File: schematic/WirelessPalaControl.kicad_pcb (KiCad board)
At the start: 2 copper layers, 26.7 x 35.1 mm, 20 parts, among them J1 6P6C, J2 MCU UART, Q1 BC847B, Q2 BC847B, U1 SI8621, U2 WeMos_mini

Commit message: Update schematic
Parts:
- C1, C2: footprint Capacitors_SMD:C_0805_HandSoldering -> Capacitor_SMD:C_0805_2012Metric_Pad1.15x1.40mm_HandSolder
- D1, D3: footprint LEDs:LED_0805_HandSoldering -> LED_SMD:LED_0805_2012Metric_Pad1.15x1.40mm_HandSolder
- D2: footprint Diodes_SMD:D_SMA -> Diode_SMD:D_SMA
- J2: footprint Pin_Headers:Pin_Header_Straight_1x04_Pitch2.54mm -> Connector_PinHeader_2.54mm:PinHeader_1x04_P2.54mm_Vertical
- Q1, Q2: footprint TO_SOT_Packages_SMD:SOT-23_Handsoldering -> Package_TO_SOT_SMD:SOT-23_Handsoldering
- R1, R2, R3, R4, R5, R6, R7, R8: footprint Resistors_SMD:R_0805_HandSoldering -> Resistor_SMD:R_0805_2012Metric_Pad1.15x1.40mm_HandSolder
- U1: footprint Housings_SOIC:SOIC-8_3.9x4.9mm_Pitch1.27mm -> Package_SO:SOIC-8_3.9x4.9mm_P1.27mm
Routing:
- net /GND2: track 40.5 -> 39.1 mm
- net Net-(D1-Pad2): track 18.5 -> 17.9 mm
- net /VDD1: track 37.8 -> 37.2 mm
- net Net-(D2-Pad1): track 15.4 -> 16.0 mm

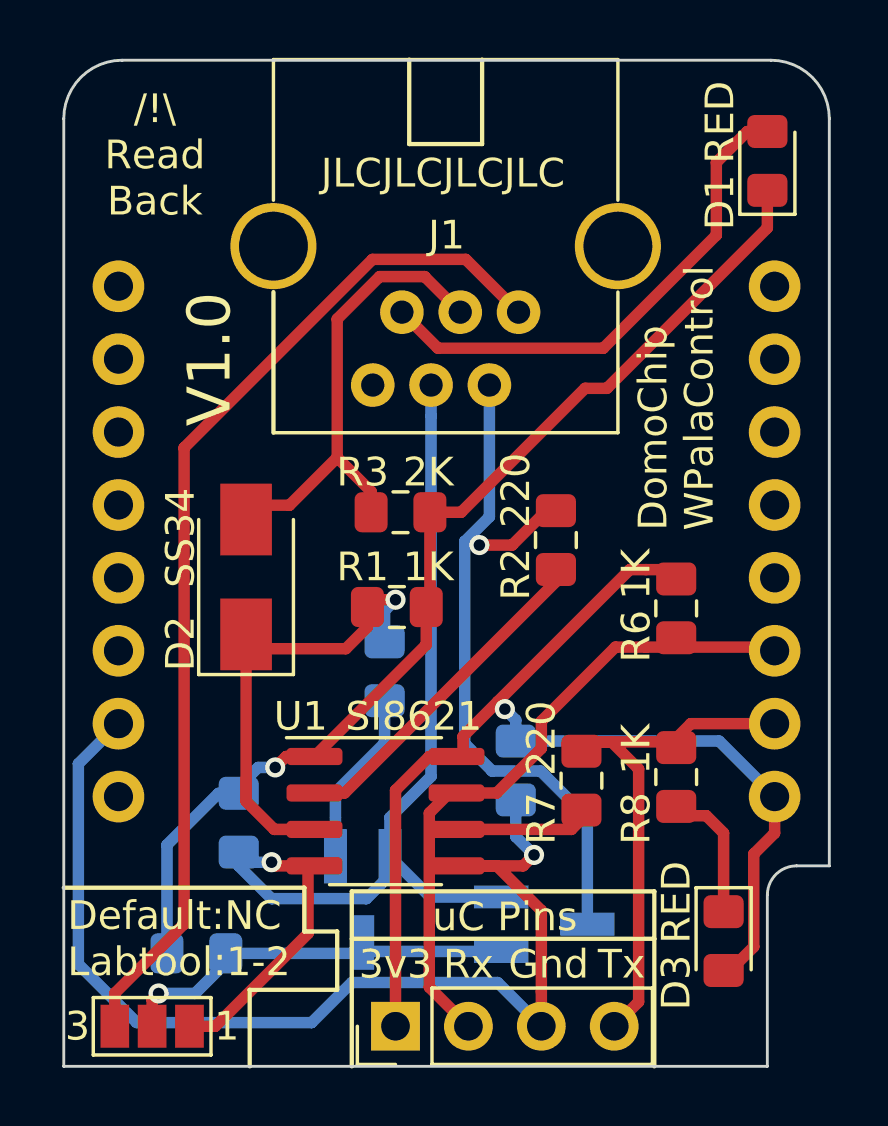
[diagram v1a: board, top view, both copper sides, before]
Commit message: Update schematic fix rj12
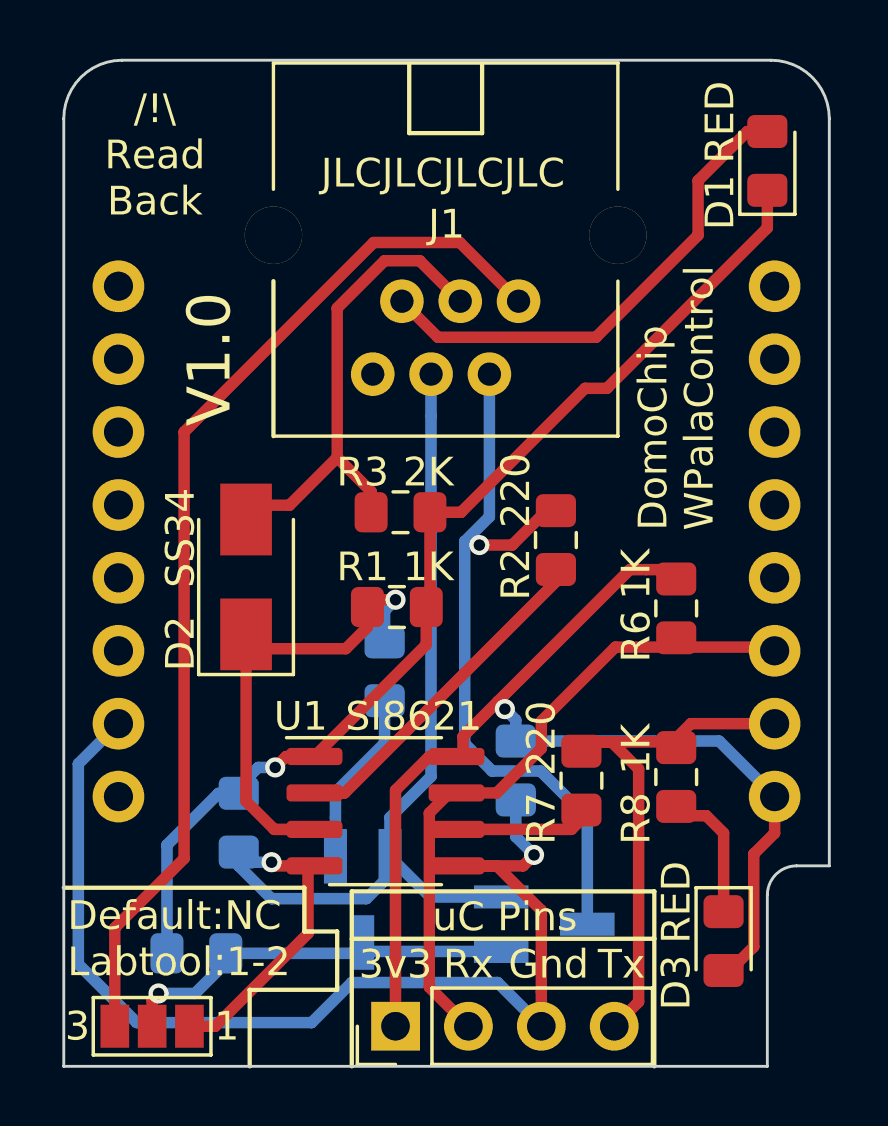
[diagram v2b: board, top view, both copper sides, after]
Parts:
- moved J1 0.38 mm to (36.2, 30.0)
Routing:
- net Net-(J1-Pad6): track 36.3 -> 36.9 mm
- net Net-(D1-Pad2): track 17.9 -> 17.3 mm
- net /Rx: track 16.5 -> 17.0 mm
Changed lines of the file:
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@@
     (add_net "Net-(R7-Pad2)")
+  )
+  (module MyRJ:Ali_RJ12 (layer F.Cu)
+    (at 36.164 29.972 180)
+    (fp_text reference J1 (at -0.031 0.381) (layer F.SilkS)
+      (effects (font (size 1 1) (thickness 0.15)))
+    )
+    (fp_text value 6P6C (at 0 1.778) (layer F.Fab)
+      (effects (font (size 1 1) (thickness 0.15)))
+    )
+    (fp_line (start 1.27 3.556) (end 1.27 6) (layer F.SilkS) (width 0.15))
+    (fp_line (start -1.27 3.556) (end 1.27 3.556) (layer F.SilkS) (width 0.15))
+    (fp_line (start -1.27 6) (end -1.27 3.556) (layer F.SilkS) (width 0.15))
+    (fp_line (start 6 -7) (end 6 -1.6) (layer F.SilkS) (width 0.15))
+    (fp_line (start -6 -7) (end -6 -1.6) (layer F.SilkS) (width 0.12))
+    (fp_line (start -6 6) (end 6 6) (layer F.SilkS) (width 0.12))
+    (fp_line (start -6 -7) (end 6 -7) (layer F.SilkS) (width 0.12))
+    (fp_line (start -6 1.6) (end -6 6) (layer F.SilkS) (width 0.12))
+    (fp_line (start 6 1.6) (end 6 6) (layer F.SilkS) (width 0.12))
+    (pad 5 thru_hole circle (at -1.524 -4.84) (size 1.52 1.52) (drill 0.81) (layers *.Cu *.Mask)
+      (net 9 /Tx-RxH))
+    (pad 1 thru_hole circle (at 2.54 -4.84) (size 1.52 1.52) (drill 0.81) (layers *.Cu *.Mask))
+    (pad 3 thru_hole circle (at 0.508 -4.84) (size 1.52 1.52) (drill 0.81) (layers *.Cu *.Mask)
+      (net 2 /GND1))
+    (pad 4 thru_hole circle (at -0.508 -2.3) (size 1.52 1.52) (drill 0.81) (layers *.Cu *.Mask)
+      (net 6 /Rx))
+    (pad 2 thru_hole circle (at 1.524 -2.3) (size 1.52 1.52) (drill 0.81) (layers *.Cu *.Mask)
+      (net 5 "Net-(D1-Pad2)"))
+    (pad 6 thru_hole circle (at -2.54 -2.3) (size 1.52 1.52) (drill 0.81) (layers *.Cu *.Mask)
+      (net 16 "Net-(J1-Pad6)"))
+    (pad "" thru_hole circle (at 6 0 180) (size 2 2) (drill 2) (layers *.Cu *.Mask))
+    (pad "" thru_hole circle (at -6 0 180) (size 2 2) (drill 2) (layers *.Cu *.Mask))
   )
   (module wemos_d1_mini:wemos-d1-mini-DIL-only (layer B.Cu)
@@
     (pad 1 smd rect (at -1.3 0 180) (size 1 1.5) (layers F.Cu F.Mask)
       (net 2 /GND1))
-  )
-  (module MyRJ:Ali_RJ12 (layer F.Cu)
-    (at 36.164 30.353 180)
-    (fp_text reference J1 (at -0.031 0.381) (layer F.SilkS)
-      (effects (font (size 1 1) (thickness 0.15)))
-    )
-    (fp_text value 6P6C (at 0 1.778) (layer F.Fab)
-      (effects (font (size 1 1) (thickness 0.15)))
-    )
-    (fp_line (start 6 1.6) (end 6 6.5) (layer F.SilkS) (width 0.12))
-    (fp_line (start -6 1.6) (end -6 6.5) (layer F.SilkS) (width 0.12))
-    (fp_line (start -6 -6.5) (end 6 -6.5) (layer F.SilkS) (width 0.12))
-    (fp_line (start -6 6.5) (end 6 6.5) (layer F.SilkS) (width 0.12))
-    (fp_line (start -6 -6.5) (end -6 -1.6) (layer F.SilkS) (width 0.12))
-    (fp_line (start 6 -6.5) (end 6 -1.6) (layer F.SilkS) (width 0.15))
-    (fp_line (start -1.27 6.5) (end -1.27 3.556) (layer F.SilkS) (width 0.15))
-    (fp_line (start -1.27 3.556) (end 1.27 3.556) (layer F.SilkS) (width 0.15))
-    (fp_line (start 1.27 3.556) (end 1.27 6.5) (layer F.SilkS) (width 0.15))
-    (pad "" np_thru_hole circle (at -6 0 180) (size 3 3) (drill 2.4) (layers *.Cu *.Mask))
-    (pad "" np_thru_hole circle (at 6 0 180) (size 3 3) (drill 2.4) (layers *.Cu *.Mask))
-    (pad 6 thru_hole circle (at -2.54 -2.3) (size 1.52 1.52) (drill 0.81) (layers *.Cu *.Mask)
-      (net 16 "Net-(J1-Pad6)"))
-    (pad 2 thru_hole circle (at 1.524 -2.3) (size 1.52 1.52) (drill 0.81) (layers *.Cu *.Mask)
-      (net 5 "Net-(D1-Pad2)"))
-    (pad 4 thru_hole circle (at -0.508 -2.3) (size 1.52 1.52) (drill 0.81) (layers *.Cu *.Mask)
-      (net 6 /Rx))
-    (pad 3 thru_hole circle (at 0.508 -4.84) (size 1.52 1.52) (drill 0.81) (layers *.Cu *.Mask)
-      (net 2 /GND1))
-    (pad 1 thru_hole circle (at 2.54 -4.84) (size 1.52 1.52) (drill 0.81) (layers *.Cu *.Mask))
-    (pad 5 thru_hole circle (at -1.524 -4.84) (size 1.52 1.52) (drill 0.81) (layers *.Cu *.Mask)
-      (net 9 /Tx-RxH))
   )
   (module Capacitor_SMD:C_0805_2012Metric_Pad1.15x1.40mm_HandSolder (layer B.Cu)
@@
   (segment (start 45.691 47.596) (end 38.608 47.596) (width 0.4) (layer B.Cu) (net 4))
   (segment (start 47.625 49.53) (end 45.691 47.596) (width 0.4) (layer B.Cu) (net 4))
-  (segment (start 34.64 32.653) (end 35.896 33.909) (width 0.4) (layer F.Cu) (net 5))
-  (segment (start 35.896 33.909) (end 41.656 33.909) (width 0.4) (layer F.Cu) (net 5))
-  (segment (start 41.656 33.909) (end 45.593 29.972) (width 0.4) (layer F.Cu) (net 5))
+  (segment (start 34.64 32.272) (end 35.896 33.528) (width 0.4) (layer F.Cu) (net 5))
+  (segment (start 35.896 33.528) (end 41.402 33.528) (width 0.4) (layer F.Cu) (net 5))
+  (segment (start 41.402 33.528) (end 44.958 29.972) (width 0.4) (layer F.Cu) (net 5))
   (segment (start 46.671 26.36) (end 47.371 26.36) (width 0.4) (layer F.Cu) (net 5))
-  (segment (start 45.593 27.438) (end 46.671 26.36) (width 0.4) (layer F.Cu) (net 5))
-  (segment (start 45.593 29.972) (end 45.593 27.438) (width 0.4) (layer F.Cu) (net 5))
-  (segment (start 36.672 32.653) (end 35.433 31.414) (width 0.4) (layer F.Cu) (net 6))
-  (segment (start 35.433 31.414) (end 33.864 31.414) (width 0.4) (layer F.Cu) (net 6))
-  (segment (start 33.864 31.414) (end 32.385 32.893) (width 0.4) (layer F.Cu) (net 6))
-  (segment (start 32.385 32.893) (end 32.385 37.718) (width 0.4) (layer F.Cu) (net 6))
+  (segment (start 44.958 28.073) (end 46.671 26.36) (width 0.4) (layer F.Cu) (net 5))
+  (segment (start 44.958 29.972) (end 44.958 28.073) (width 0.4) (layer F.Cu) (net 5))
   (segment (start 33.566 38.899) (end 33.566 39.624) (width 0.4) (layer F.Cu) (net 6))
   (segment (start 32.385 37.718) (end 33.566 38.899) (width 0.4) (layer F.Cu) (net 6))
   (segment (start 30.725 39.378) (end 29.21 39.378) (width 0.4) (layer F.Cu) (net 6))
   (segment (start 32.385 37.718) (end 30.725 39.378) (width 0.4) (layer F.Cu) (net 6))
+  (segment (start 36.672 32.272) (end 35.261 30.861) (width 0.4) (layer F.Cu) (net 6))
+  (segment (start 35.261 30.861) (end 34.036 30.861) (width 0.4) (layer F.Cu) (net 6))
+  (segment (start 32.385 32.512) (end 32.385 37.718) (width 0.4) (layer F.Cu) (net 6))
+  (segment (start 34.036 30.861) (end 32.385 32.512) (width 0.4) (layer F.Cu) (net 6))
   (segment (start 30.194 50.673) (end 31.369 50.673) (width 0.4) (layer F.Cu) (net 7))
   (segment (start 29.21 49.689) (end 30.194 50.673) (width 0.4) (layer F.Cu) (net 7))
@@
   (segment (start 40.546 50.673) (end 40.894 50.325) (width 0.4) (layer F.Cu) (net 15))
   (segment (start 36.769 50.673) (end 40.546 50.673) (width 0.4) (layer F.Cu) (net 15))
-  (segment (start 33.615467 30.813991) (end 27.051 37.378458) (width 0.4) (layer F.Cu) (net 16))
-  (segment (start 38.704 32.653) (end 36.864991 30.813991) (width 0.4) (layer F.Cu) (net 16))
-  (segment (start 36.864991 30.813991) (end 33.615467 30.813991) (width 0.4) (layer F.Cu) (net 16))
-  (segment (start 24.638 56.381) (end 24.638 57.531) (width 0.4) (layer F.Cu) (net 16))
-  (segment (start 27.051 53.968) (end 24.638 56.381) (width 0.4) (layer F.Cu) (net 16))
-  (segment (start 27.051 37.378458) (end 27.051 53.968) (width 0.4) (layer F.Cu) (net 16))
+  (segment (start 38.704 32.272) (end 36.658 30.226) (width 0.4) (layer F.Cu) (net 16))
+  (segment (start 36.658 30.226) (end 33.655 30.226) (width 0.4) (layer F.Cu) (net 16))
+  (segment (start 33.655 30.226) (end 27.051 36.83) (width 0.4) (layer F.Cu) (net 16))
+  (segment (start 27.051 36.83) (end 27.051 51.689) (width 0.4) (layer F.Cu) (net 16))
+  (segment (start 24.638 54.102) (end 24.638 57.531) (width 0.4) (layer F.Cu) (net 16))
+  (segment (start 27.051 51.689) (end 24.638 54.102) (width 0.4) (layer F.Cu) (net 16))
 )

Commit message: Update PCB fix size V1.1
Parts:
- moved D1 2.41 mm to (45.5, 25.9), turned to 180 degrees
- moved JP1 1.88 mm to (27.8, 57.4)
- moved C2 1.39 mm to (38.6, 47.2)
- moved R4 1.05 mm to (34.0, 46.2)
- moved R3 1.02 mm to (34.5, 40.6)
- moved R7 0.96 mm to (40.9, 48.0)
- moved R2 0.93 mm to (40.0, 41.5)
- moved R1 0.89 mm to (34.5, 43.8)
- moved R8 0.83 mm to (44.2, 48.0)
- moved J1 0.76 mm to (36.2, 30.7)
- moved Q2 0.63 mm to (39.6, 53.3)
- moved R5 0.51 mm to (27.5, 55.5)
- moved Q1 0.43 mm to (33.3, 52.7)
- moved J2 0.40 mm to (34.3, 57.1)
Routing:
- net /VDD2: track 39.9 -> 42.3 mm, vias 1 -> 2
- net /Tx-RxH: track 25.8 -> 23.5 mm
- net /VDD1: track 37.2 -> 39.1 mm
- net /GND1: track 38.8 -> 37.4 mm
- net Net-(J1-Pad6): track 36.9 -> 35.6 mm
- net Net-(D3-Pad1): track 4.31 -> 5.59 mm
- net /GND2: track 39.1 -> 40.3 mm
- net /RXuC: track 23.0 -> 23.9 mm
- net Net-(Q1-Pad1): track 5.80 -> 5.03 mm
- net Net-(R7-Pad2): track 4.27 -> 5.03 mm
- net /Q2B: track 14.0 -> 13.3 mm
- net Net-(R2-Pad2): track 11.8 -> 11.3 mm
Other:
- board size 26.7 x 35.1 mm -> 25.4 x 33.7 mm
- board text added: "!!!"
- board text added: "DomoChip WPalaControl V1.1"
- board text added: "Read Back !!!"
- board text added: "Use RJ11 cross cable (phone standard)"
- board text added: "V1.1"
- board text removed: "/!\ Read Back"
- board text removed: "/!\ Use RJ11 cross cable (phone standard) /!\"
- board text removed: "DomoChip WPalaControl V1.0"
- board text removed: "V1.0"
